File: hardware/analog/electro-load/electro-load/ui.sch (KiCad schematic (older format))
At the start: 5 parts, among them U5 RC1602A

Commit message: HW rev 1 of electronic load PCB.
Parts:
- removed D3: STATUS, LED_THT:LED_D5.0mm-4_RGB_Wide_Pins, symbol Device:LED_ABRG
- removed R21: 200, Resistor_SMD:R_0603_1608Metric, symbol Device:R_Small
- added C18, C19, C20: 100n, Capacitor_SMD:C_0603_1608Metric, symbol Device:C_Small
- added R33, R34, R35: 10k, Resistor_SMD:R_0603_1608Metric, symbol Device:R_Small
- added SW2: Rotary_Encoder_Switch, Rotary_Encoder:RotaryEncoder_Alps_EC11E-Switch_Vertical_H20mm, symbol Device:Rotary_Encoder_Switch
- renumbered R22 to R16, R23 to R17
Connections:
- net labels added: ROT_A, ROT_B, ROT_SW
- net labels removed: STATUS_B, STATUS_G, STATUS_R
- wire segments 12 -> 34
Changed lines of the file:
@@
 EESchema Schematic File Version 4
-LIBS:electro-load-cache
 EELAYER 30 0
 EELAYER END
@@
 $EndDescr
 $Comp
-L Device:LED_ABRG D?
-U 1 1 5E7F5ED6
-P 2400 2125
-AR Path="/5E7F5ED6" Ref="D?"  Part="1"
-AR Path="/5E7EC7EF/5E7F5ED6" Ref="D3"  Part="1"
-F 0 "D3" V 2446 1795 50  0000 R CNN
-F 1 "STATUS" V 2355 1795 50  0000 R CNN
-F 2 "LED_THT:LED_D5.0mm-4_RGB_Wide_Pins" H 2400 2125 50  0001 C CNN
-F 3 "~" H 2400 2125 50  0001 C CNN
-	1    2400 2125
-	0    -1   -1   0
-$EndComp
-$Comp
-L Device:R_Small R?
-U 1 1 5E7F5EDC
-P 2400 1725
-AR Path="/5E7F5EDC" Ref="R?"  Part="1"
-AR Path="/5E7EC7EF/5E7F5EDC" Ref="R21"  Part="1"
-F 0 "R21" H 2459 1771 50  0000 L CNN
-F 1 "200" H 2459 1680 50  0000 L CNN
-F 2 "Resistor_SMD:R_0603_1608Metric" H 2400 1725 50  0001 C CNN
-F 3 "~" H 2400 1725 50  0001 C CNN
-	1    2400 1725
-	1    0    0    -1
-$EndComp
-Wire Wire Line
-	2400 1825 2400 1925
-$Comp
-L power:+5V #PWR?
-U 1 1 5E7F5EE3
-P 2400 1600
-AR Path="/5E7F5EE3" Ref="#PWR?"  Part="1"
-AR Path="/5E7EC7EF/5E7F5EE3" Ref="#PWR041"  Part="1"
-F 0 "#PWR041" H 2400 1450 50  0001 C CNN
-F 1 "+5V" H 2415 1773 50  0000 C CNN
-F 2 "" H 2400 1600 50  0001 C CNN
-F 3 "" H 2400 1600 50  0001 C CNN
-	1    2400 1600
-	1    0    0    -1
-$EndComp
-Wire Wire Line
-	2400 1600 2400 1625
-Text Label 2200 2325 3    50   ~ 0
-STATUS_R
-Text Label 2400 2325 3    50   ~ 0
-STATUS_G
-Text Label 2600 2325 3    50   ~ 0
-STATUS_B
-$Comp
 L athir:RC1602A U?
 U 1 1 5E8030BB
@@
 	1    0    0    -1
 $EndComp
-Text Label 4575 1825 2    50   ~ 0
-LCD_RS
-Text Label 4575 1925 2    50   ~ 0
-LCD_RW
-Text Label 4575 2025 2    50   ~ 0
-LCD_EN
-Text Label 4575 2825 2    50   ~ 0
-LCD_DB7
-Text Label 4575 2725 2    50   ~ 0
-LCD_DB6
-Text Label 4575 2625 2    50   ~ 0
-LCD_DB5
-Text Label 4575 2525 2    50   ~ 0
-LCD_DB4
 NoConn ~ 4575 2125
 NoConn ~ 4575 2225
@@
 P 4975 3050
 AR Path="/5E8030CC" Ref="#PWR?"  Part="1"
-AR Path="/5E7EC7EF/5E8030CC" Ref="#PWR043"  Part="1"
-F 0 "#PWR043" H 4975 2800 50  0001 C CNN
+AR Path="/5E7EC7EF/5E8030CC" Ref="#PWR038"  Part="1"
+F 0 "#PWR038" H 4975 2800 50  0001 C CNN
 F 1 "GND" H 4980 2877 50  0000 C CNN
 F 2 "" H 4975 3050 50  0001 C CNN
@@
 P 4975 1575
 AR Path="/5E8030D3" Ref="#PWR?"  Part="1"
-AR Path="/5E7EC7EF/5E8030D3" Ref="#PWR042"  Part="1"
-F 0 "#PWR042" H 4975 1425 50  0001 C CNN
+AR Path="/5E7EC7EF/5E8030D3" Ref="#PWR037"  Part="1"
+F 0 "#PWR037" H 4975 1425 50  0001 C CNN
 F 1 "+5V" H 4990 1748 50  0000 C CNN
 F 2 "" H 4975 1575 50  0001 C CNN
@@
 P 5575 2125
 AR Path="/5E8030DA" Ref="R?"  Part="1"
-AR Path="/5E7EC7EF/5E8030DA" Ref="R22"  Part="1"
-F 0 "R22" V 5379 2125 50  0000 C CNN
+AR Path="/5E7EC7EF/5E8030DA" Ref="R16"  Part="1"
+F 0 "R16" V 5379 2125 50  0000 C CNN
 F 1 "2k" V 5470 2125 50  0000 C CNN
 F 2 "Resistor_SMD:R_0603_1608Metric" H 5575 2125 50  0001 C CNN
@@
 P 5600 2625
 AR Path="/5E8030E0" Ref="R?"  Part="1"
-AR Path="/5E7EC7EF/5E8030E0" Ref="R23"  Part="1"
-F 0 "R23" V 5404 2625 50  0000 C CNN
+AR Path="/5E7EC7EF/5E8030E0" Ref="R17"  Part="1"
+F 0 "R17" V 5404 2625 50  0000 C CNN
 F 1 "220" V 5495 2625 50  0000 C CNN
 F 2 "Resistor_SMD:R_0603_1608Metric" H 5600 2625 50  0001 C CNN
@@
 P 5450 2700
 AR Path="/5E8030E6" Ref="#PWR?"  Part="1"
-AR Path="/5E7EC7EF/5E8030E6" Ref="#PWR044"  Part="1"
-F 0 "#PWR044" H 5450 2450 50  0001 C CNN
+AR Path="/5E7EC7EF/5E8030E6" Ref="#PWR039"  Part="1"
+F 0 "#PWR039" H 5450 2450 50  0001 C CNN
 F 1 "GND" H 5455 2527 50  0000 C CNN
 F 2 "" H 5450 2700 50  0001 C CNN
@@
 P 5725 2200
 AR Path="/5E8030F0" Ref="#PWR?"  Part="1"
-AR Path="/5E7EC7EF/5E8030F0" Ref="#PWR045"  Part="1"
-F 0 "#PWR045" H 5725 1950 50  0001 C CNN
+AR Path="/5E7EC7EF/5E8030F0" Ref="#PWR040"  Part="1"
+F 0 "#PWR040" H 5725 1950 50  0001 C CNN
 F 1 "GND" H 5730 2027 50  0000 C CNN
 F 2 "" H 5725 2200 50  0001 C CNN
@@
 P 5800 2575
 AR Path="/5E8030F8" Ref="#PWR?"  Part="1"
-AR Path="/5E7EC7EF/5E8030F8" Ref="#PWR046"  Part="1"
-F 0 "#PWR046" H 5800 2425 50  0001 C CNN
+AR Path="/5E7EC7EF/5E8030F8" Ref="#PWR041"  Part="1"
+F 0 "#PWR041" H 5800 2425 50  0001 C CNN
 F 1 "+5V" H 5815 2748 50  0000 C CNN
 F 2 "" H 5800 2575 50  0001 C CNN
@@
 Wire Wire Line
 	5800 2625 5700 2625
+Text HLabel 4575 1825 0    50   Input ~ 0
+LCD_RS
+Text HLabel 4575 1925 0    50   Input ~ 0
+LCD_RW
+Text HLabel 4575 2025 0    50   Input ~ 0
+LCD_EN
+Text HLabel 4575 2525 0    50   Input ~ 0
+LCD_DB4
+Text HLabel 4575 2625 0    50   Input ~ 0
+LCD_DB5
+Text HLabel 4575 2725 0    50   Input ~ 0
+LCD_DB6
+Text HLabel 4575 2825 0    50   Input ~ 0
+LCD_DB7
+$Comp
+L Device:Rotary_Encoder_Switch SW2
+U 1 1 5E83A7B7
+P 2550 2950
+F 0 "SW2" H 2550 3317 50  0000 C CNN
+F 1 "Rotary_Encoder_Switch" H 2550 3226 50  0000 C CNN
+F 2 "Rotary_Encoder:RotaryEncoder_Alps_EC11E-Switch_Vertical_H20mm" H 2400 3110 50  0001 C CNN
+F 3 "~" H 2550 3210 50  0001 C CNN
+	1    2550 2950
+	1    0    0    -1
+$EndComp
+$Comp
+L power:GND #PWR0102
+U 1 1 5E842AD8
+P 2100 3425
+F 0 "#PWR0102" H 2100 3175 50  0001 C CNN
+F 1 "GND" H 2105 3252 50  0000 C CNN
+F 2 "" H 2100 3425 50  0001 C CNN
+F 3 "" H 2100 3425 50  0001 C CNN
+	1    2100 3425
+	1    0    0    -1
+$EndComp
+Wire Wire Line
+	2250 2950 2100 2950
+Wire Wire Line
+	2100 2950 2100 3375
+$Comp
+L Device:R_Small R?
+U 1 1 5E8431F3
+P 1875 3050
+AR Path="/5E8431F3" Ref="R?"  Part="1"
+AR Path="/5E7EC7EF/5E8431F3" Ref="R34"  Part="1"
+F 0 "R34" H 1934 3096 50  0000 L CNN
+F 1 "10k" H 1934 3005 50  0000 L CNN
+F 2 "Resistor_SMD:R_0603_1608Metric" H 1875 3050 50  0001 C CNN
+F 3 "~" H 1875 3050 50  0001 C CNN
+	1    1875 3050
+	0    1    1    0
+$EndComp
+Wire Wire Line
+	1975 3050 2250 3050
+$Comp
+L Device:R_Small R?
+U 1 1 5E843CAF
+P 1875 2850
+AR Path="/5E843CAF" Ref="R?"  Part="1"
+AR Path="/5E7EC7EF/5E843CAF" Ref="R33"  Part="1"
+F 0 "R33" H 1934 2896 50  0000 L CNN
+F 1 "10k" H 1934 2805 50  0000 L CNN
+F 2 "Resistor_SMD:R_0603_1608Metric" H 1875 2850 50  0001 C CNN
+F 3 "~" H 1875 2850 50  0001 C CNN
+	1    1875 2850
+	0    1    1    0
+$EndComp
+Wire Wire Line
+	1975 2850 2250 2850
+$Comp
+L Device:C_Small C19
+U 1 1 5E844730
+P 1600 3225
+F 0 "C19" H 1692 3271 50  0000 L CNN
+F 1 "100n" H 1600 3150 50  0000 L CNN
+F 2 "Capacitor_SMD:C_0603_1608Metric" H 1600 3225 50  0001 C CNN
+F 3 "~" H 1600 3225 50  0001 C CNN
+	1    1600 3225
+	1    0    0    -1
+$EndComp
+Wire Wire Line
+	1600 3125 1600 3050
+Wire Wire Line
+	1600 3050 1775 3050
+$Comp
+L Device:C_Small C18
+U 1 1 5E844FE5
+P 1375 3225
+F 0 "C18" H 1467 3271 50  0000 L CNN
+F 1 "100n" H 1275 3150 50  0000 L CNN
+F 2 "Capacitor_SMD:C_0603_1608Metric" H 1375 3225 50  0001 C CNN
+F 3 "~" H 1375 3225 50  0001 C CNN
+	1    1375 3225
+	1    0    0    -1
+$EndComp
+Wire Wire Line
+	1775 2850 1375 2850
+Wire Wire Line
+	1375 2850 1375 3125
+Wire Wire Line
+	2100 3375 1600 3375
+Wire Wire Line
+	1600 3375 1600 3325
+Connection ~ 2100 3375
+Wire Wire Line
+	2100 3375 2100 3425
+Wire Wire Line
+	1600 3375 1375 3375
+Wire Wire Line
+	1375 3375 1375 3325
+Connection ~ 1600 3375
+$Comp
+L Device:R_Small R?
+U 1 1 5E848965
+P 3075 2850
+AR Path="/5E848965" Ref="R?"  Part="1"
+AR Path="/5E7EC7EF/5E848965" Ref="R35"  Part="1"
+F 0 "R35" H 3134 2896 50  0000 L CNN
+F 1 "10k" H 3134 2805 50  0000 L CNN
+F 2 "Resistor_SMD:R_0603_1608Metric" H 3075 2850 50  0001 C CNN
+F 3 "~" H 3075 2850 50  0001 C CNN
+	1    3075 2850
+	0    1    1    0
+$EndComp
+Wire Wire Line
+	2975 2850 2850 2850
+$Comp
+L power:GND #PWR0103
+U 1 1 5E84951B
+P 2925 3175
+F 0 "#PWR0103" H 2925 2925 50  0001 C CNN
+F 1 "GND" H 2930 3002 50  0000 C CNN
+F 2 "" H 2925 3175 50  0001 C CNN
+F 3 "" H 2925 3175 50  0001 C CNN
+	1    2925 3175
+	1    0    0    -1
+$EndComp
+Wire Wire Line
+	2925 3175 2925 3150
+Wire Wire Line
+	2925 3050 2850 3050
+$Comp
+L Device:C_Small C20
+U 1 1 5E84BAE6
+P 3275 3025
+F 0 "C20" H 3367 3071 50  0000 L CNN
+F 1 "100n" H 3275 2950 50  0000 L CNN
+F 2 "Capacitor_SMD:C_0603_1608Metric" H 3275 3025 50  0001 C CNN
+F 3 "~" H 3275 3025 50  0001 C CNN
+	1    3275 3025
+	1    0    0    -1
+$EndComp
+Wire Wire Line
+	3275 2925 3275 2850
+Wire Wire Line
+	3275 2850 3175 2850
+Wire Wire Line
+	3275 3125 3275 3150
+Wire Wire Line
+	3275 3150 2925 3150
+Connection ~ 2925 3150
+Wire Wire Line
+	2925 3150 2925 3050
+Text HLabel 3375 2850 2    50   Input ~ 0
+ROT_SW
+Wire Wire Line
+	3375 2850 3275 2850
+Connection ~ 3275 2850
+Text HLabel 1300 2850 0    50   Input ~ 0
+ROT_A
+Wire Wire Line
+	1300 2850 1375 2850
+Connection ~ 1375 2850
+Text HLabel 1275 3050 0    50   Input ~ 0
+ROT_B
+Wire Wire Line
+	1275 3050 1600 3050
+Connection ~ 1600 3050
 $EndSCHEMATC

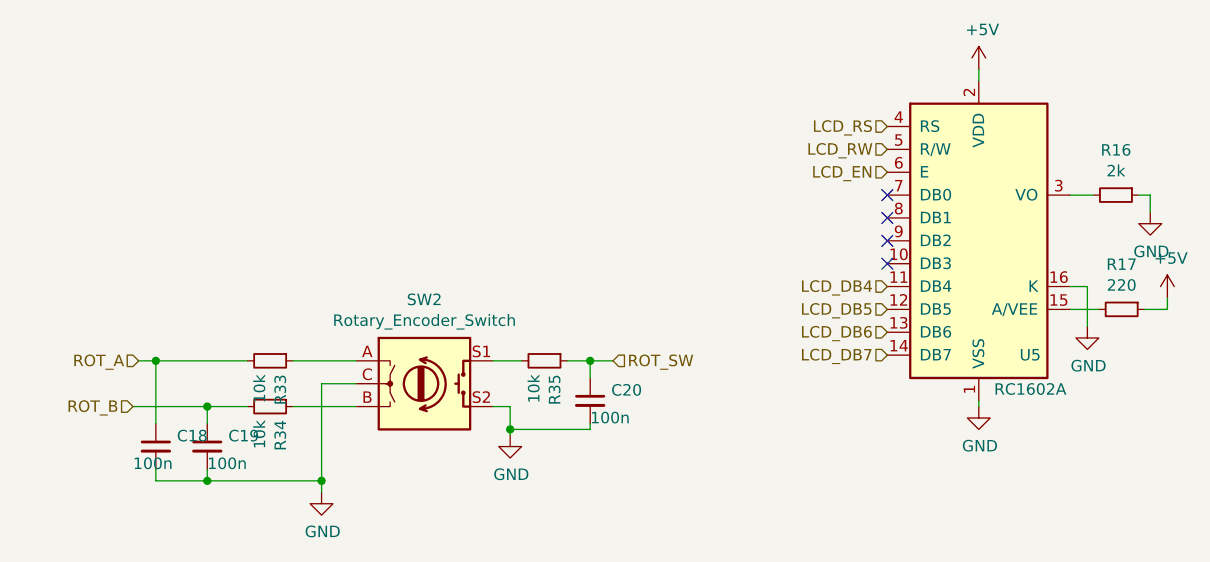
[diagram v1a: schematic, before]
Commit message: Added voltage reference REF5020 datasheet
Started work on HW rev 2 of electro load and 5v-from-mains - rev 1 contained misaligned footprints.
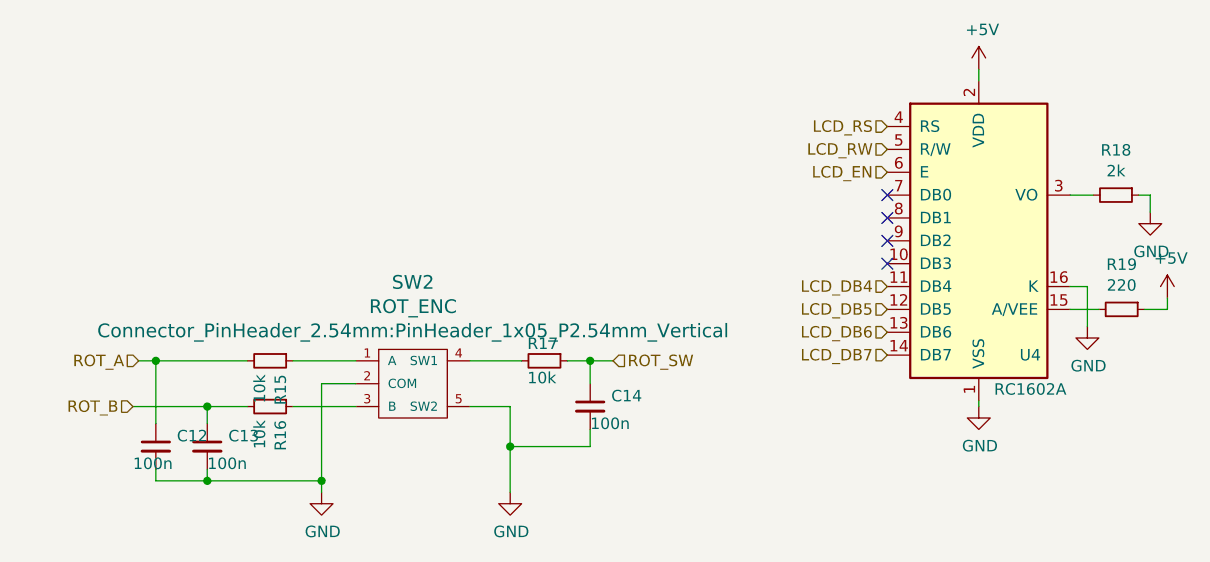
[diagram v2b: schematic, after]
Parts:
- removed SW2: Rotary_Encoder_Switch, Rotary_Encoder:RotaryEncoder_Alps_EC11E-Switch_Vertical_H20mm, symbol Device:Rotary_Encoder_Switch
- added SW2: ROT_ENC, Connector_PinHeader_2.54mm:PinHeader_1x05_P2.54mm_Vertical, symbol athir:ROT_ENC_SW
- renumbered C18 to C12, C19 to C13, C20 to C14, R33 to R15, R34 to R16, R35 to R17, R16 to R18, R17 to R19, U5 to U4
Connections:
- net GND: now also SW2.2 (COM), SW2.5 (SW2)
- net at R15.1: now also SW2.1 (A)
- net at R16.1: now also SW2.3 (B)
- net at R17.2: now also SW2.4 (SW1)
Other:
- moved on the sheet: C14
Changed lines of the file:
@@
 P 4975 2325
 AR Path="/5E8030BB" Ref="U?"  Part="1"
-AR Path="/5E7EC7EF/5E8030BB" Ref="U5"  Part="1"
-F 0 "U5" H 5200 1825 50  0000 C CNN
+AR Path="/5E7EC7EF/5E8030BB" Ref="U4"  Part="1"
+F 0 "U4" H 5200 1825 50  0000 C CNN
 F 1 "RC1602A" H 5200 1675 50  0000 C CNN
 F 2 "Connector_PinHeader_2.54mm:PinHeader_1x16_P2.54mm_Vertical" H 5075 1525 50  0001 C CNN
@@
 P 4975 3050
 AR Path="/5E8030CC" Ref="#PWR?"  Part="1"
-AR Path="/5E7EC7EF/5E8030CC" Ref="#PWR038"  Part="1"
-F 0 "#PWR038" H 4975 2800 50  0001 C CNN
+AR Path="/5E7EC7EF/5E8030CC" Ref="#PWR034"  Part="1"
+F 0 "#PWR034" H 4975 2800 50  0001 C CNN
 F 1 "GND" H 4980 2877 50  0000 C CNN
 F 2 "" H 4975 3050 50  0001 C CNN
@@
 P 4975 1575
 AR Path="/5E8030D3" Ref="#PWR?"  Part="1"
-AR Path="/5E7EC7EF/5E8030D3" Ref="#PWR037"  Part="1"
-F 0 "#PWR037" H 4975 1425 50  0001 C CNN
+AR Path="/5E7EC7EF/5E8030D3" Ref="#PWR033"  Part="1"
+F 0 "#PWR033" H 4975 1425 50  0001 C CNN
 F 1 "+5V" H 4990 1748 50  0000 C CNN
 F 2 "" H 4975 1575 50  0001 C CNN
@@
 P 5575 2125
 AR Path="/5E8030DA" Ref="R?"  Part="1"
-AR Path="/5E7EC7EF/5E8030DA" Ref="R16"  Part="1"
-F 0 "R16" V 5379 2125 50  0000 C CNN
+AR Path="/5E7EC7EF/5E8030DA" Ref="R18"  Part="1"
+F 0 "R18" V 5379 2125 50  0000 C CNN
 F 1 "2k" V 5470 2125 50  0000 C CNN
 F 2 "Resistor_SMD:R_0603_1608Metric" H 5575 2125 50  0001 C CNN
@@
 P 5600 2625
 AR Path="/5E8030E0" Ref="R?"  Part="1"
-AR Path="/5E7EC7EF/5E8030E0" Ref="R17"  Part="1"
-F 0 "R17" V 5404 2625 50  0000 C CNN
+AR Path="/5E7EC7EF/5E8030E0" Ref="R19"  Part="1"
+F 0 "R19" V 5404 2625 50  0000 C CNN
 F 1 "220" V 5495 2625 50  0000 C CNN
 F 2 "Resistor_SMD:R_0603_1608Metric" H 5600 2625 50  0001 C CNN
@@
 P 5450 2700
 AR Path="/5E8030E6" Ref="#PWR?"  Part="1"
-AR Path="/5E7EC7EF/5E8030E6" Ref="#PWR039"  Part="1"
-F 0 "#PWR039" H 5450 2450 50  0001 C CNN
+AR Path="/5E7EC7EF/5E8030E6" Ref="#PWR035"  Part="1"
+F 0 "#PWR035" H 5450 2450 50  0001 C CNN
 F 1 "GND" H 5455 2527 50  0000 C CNN
 F 2 "" H 5450 2700 50  0001 C CNN
@@
 P 5725 2200
 AR Path="/5E8030F0" Ref="#PWR?"  Part="1"
-AR Path="/5E7EC7EF/5E8030F0" Ref="#PWR040"  Part="1"
-F 0 "#PWR040" H 5725 1950 50  0001 C CNN
+AR Path="/5E7EC7EF/5E8030F0" Ref="#PWR036"  Part="1"
+F 0 "#PWR036" H 5725 1950 50  0001 C CNN
 F 1 "GND" H 5730 2027 50  0000 C CNN
 F 2 "" H 5725 2200 50  0001 C CNN
@@
 P 5800 2575
 AR Path="/5E8030F8" Ref="#PWR?"  Part="1"
-AR Path="/5E7EC7EF/5E8030F8" Ref="#PWR041"  Part="1"
-F 0 "#PWR041" H 5800 2425 50  0001 C CNN
+AR Path="/5E7EC7EF/5E8030F8" Ref="#PWR037"  Part="1"
+F 0 "#PWR037" H 5800 2425 50  0001 C CNN
 F 1 "+5V" H 5815 2748 50  0000 C CNN
 F 2 "" H 5800 2575 50  0001 C CNN
@@
 LCD_DB7
 $Comp
-L Device:Rotary_Encoder_Switch SW2
-U 1 1 5E83A7B7
-P 2550 2950
-F 0 "SW2" H 2550 3317 50  0000 C CNN
-F 1 "Rotary_Encoder_Switch" H 2550 3226 50  0000 C CNN
-F 2 "Rotary_Encoder:RotaryEncoder_Alps_EC11E-Switch_Vertical_H20mm" H 2400 3110 50  0001 C CNN
-F 3 "~" H 2550 3210 50  0001 C CNN
-	1    2550 2950
-	1    0    0    -1
-$EndComp
-$Comp
-L power:GND #PWR0102
+L power:GND #PWR031
 U 1 1 5E842AD8
 P 2100 3425
-F 0 "#PWR0102" H 2100 3175 50  0001 C CNN
+F 0 "#PWR031" H 2100 3175 50  0001 C CNN
 F 1 "GND" H 2105 3252 50  0000 C CNN
 F 2 "" H 2100 3425 50  0001 C CNN
@@
 P 1875 3050
 AR Path="/5E8431F3" Ref="R?"  Part="1"
-AR Path="/5E7EC7EF/5E8431F3" Ref="R34"  Part="1"
-F 0 "R34" H 1934 3096 50  0000 L CNN
+AR Path="/5E7EC7EF/5E8431F3" Ref="R16"  Part="1"
+F 0 "R16" H 1934 3096 50  0000 L CNN
 F 1 "10k" H 1934 3005 50  0000 L CNN
 F 2 "Resistor_SMD:R_0603_1608Metric" H 1875 3050 50  0001 C CNN
@@
 P 1875 2850
 AR Path="/5E843CAF" Ref="R?"  Part="1"
-AR Path="/5E7EC7EF/5E843CAF" Ref="R33"  Part="1"
-F 0 "R33" H 1934 2896 50  0000 L CNN
+AR Path="/5E7EC7EF/5E843CAF" Ref="R15"  Part="1"
+F 0 "R15" H 1934 2896 50  0000 L CNN
 F 1 "10k" H 1934 2805 50  0000 L CNN
 F 2 "Resistor_SMD:R_0603_1608Metric" H 1875 2850 50  0001 C CNN
@@
 	1975 2850 2250 2850
 $Comp
-L Device:C_Small C19
+L Device:C_Small C13
 U 1 1 5E844730
 P 1600 3225
-F 0 "C19" H 1692 3271 50  0000 L CNN
+F 0 "C13" H 1692 3271 50  0000 L CNN
 F 1 "100n" H 1600 3150 50  0000 L CNN
 F 2 "Capacitor_SMD:C_0603_1608Metric" H 1600 3225 50  0001 C CNN
@@
 	1600 3050 1775 3050
 $Comp
-L Device:C_Small C18
+L Device:C_Small C12
 U 1 1 5E844FE5
 P 1375 3225
-F 0 "C18" H 1467 3271 50  0000 L CNN
+F 0 "C12" H 1467 3271 50  0000 L CNN
 F 1 "100n" H 1275 3150 50  0000 L CNN
 F 2 "Capacitor_SMD:C_0603_1608Metric" H 1375 3225 50  0001 C CNN
@@
 P 3075 2850
 AR Path="/5E848965" Ref="R?"  Part="1"
-AR Path="/5E7EC7EF/5E848965" Ref="R35"  Part="1"
-F 0 "R35" H 3134 2896 50  0000 L CNN
-F 1 "10k" H 3134 2805 50  0000 L CNN
+AR Path="/5E7EC7EF/5E848965" Ref="R17"  Part="1"
+F 0 "R17" V 3000 2775 50  0000 L CNN
+F 1 "10k" V 3150 2775 50  0000 L CNN
 F 2 "Resistor_SMD:R_0603_1608Metric" H 3075 2850 50  0001 C CNN
 F 3 "~" H 3075 2850 50  0001 C CNN
@@
 	0    1    1    0
 $EndComp
-Wire Wire Line
-	2975 2850 2850 2850
-$Comp
-L power:GND #PWR0103
+$Comp
+L power:GND #PWR032
 U 1 1 5E84951B
-P 2925 3175
-F 0 "#PWR0103" H 2925 2925 50  0001 C CNN
-F 1 "GND" H 2930 3002 50  0000 C CNN
-F 2 "" H 2925 3175 50  0001 C CNN
-F 3 "" H 2925 3175 50  0001 C CNN
-	1    2925 3175
-	1    0    0    -1
-$EndComp
-Wire Wire Line
-	2925 3175 2925 3150
-Wire Wire Line
-	2925 3050 2850 3050
-$Comp
-L Device:C_Small C20
+P 2925 3425
+F 0 "#PWR032" H 2925 3175 50  0001 C CNN
+F 1 "GND" H 2930 3252 50  0000 C CNN
+F 2 "" H 2925 3425 50  0001 C CNN
+F 3 "" H 2925 3425 50  0001 C CNN
+	1    2925 3425
+	1    0    0    -1
+$EndComp
+Wire Wire Line
+	2925 3425 2925 3225
+$Comp
+L Device:C_Small C14
 U 1 1 5E84BAE6
-P 3275 3025
-F 0 "C20" H 3367 3071 50  0000 L CNN
-F 1 "100n" H 3275 2950 50  0000 L CNN
-F 2 "Capacitor_SMD:C_0603_1608Metric" H 3275 3025 50  0001 C CNN
-F 3 "~" H 3275 3025 50  0001 C CNN
-	1    3275 3025
-	1    0    0    -1
-$EndComp
-Wire Wire Line
-	3275 2925 3275 2850
+P 3275 3050
+F 0 "C14" H 3367 3096 50  0000 L CNN
+F 1 "100n" H 3275 2975 50  0000 L CNN
+F 2 "Capacitor_SMD:C_0603_1608Metric" H 3275 3050 50  0001 C CNN
+F 3 "~" H 3275 3050 50  0001 C CNN
+	1    3275 3050
+	1    0    0    -1
+$EndComp
+Wire Wire Line
+	3275 2950 3275 2850
 Wire Wire Line
 	3275 2850 3175 2850
 Wire Wire Line
-	3275 3125 3275 3150
-Wire Wire Line
-	3275 3150 2925 3150
-Connection ~ 2925 3150
-Wire Wire Line
-	2925 3150 2925 3050
+	3275 3150 3275 3225
+Wire Wire Line
+	3275 3225 2925 3225
+Connection ~ 2925 3225
+Wire Wire Line
+	2925 3225 2925 3050
 Text HLabel 3375 2850 2    50   Input ~ 0
 ROT_SW
@@
 	1275 3050 1600 3050
 Connection ~ 1600 3050
+$Comp
+L athir:ROT_ENC_SW SW2
+U 1 1 5E990CCA
+P 2450 2950
+F 0 "SW2" H 2500 3393 60  0000 C CNN
+F 1 "ROT_ENC" H 2500 3287 60  0000 C CNN
+F 2 "Connector_PinHeader_2.54mm:PinHeader_1x05_P2.54mm_Vertical" H 2500 3181 60  0000 C CNN
+F 3 "" H 2450 2950 60  0000 C CNN
+	1    2450 2950
+	1    0    0    -1
+$EndComp
+Wire Wire Line
+	2750 2850 2975 2850
+Wire Wire Line
+	2750 3050 2925 3050
 $EndSCHEMATC
